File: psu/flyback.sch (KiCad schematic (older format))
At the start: 74 parts

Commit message: Annotate
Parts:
- gave numbers to parts that had none: 74

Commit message: Start PCB
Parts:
- added TP206, TP207: TESTPAD, agg:SIL-254P-01, symbol agg:TESTPAD
- C201: footprint agg:0603 -> agg:1206; Farnell 2320814 -> 1759454; Voltage 16V -> 50V
- C214: value DNF -> 10n; Farnell (none) -> 2896776
- D201, D202: footprint (none) -> agg:SOD-123
- R201, R205: Farnell 2145283 -> 2079442
- R204: value DNF -> 4R7; Farnell (none) -> 2447524
- R213, R214, R215, R216, R222, R223, R224, R225: footprint agg:0805 -> agg:1206; Farnell 2447667 -> 2695162; Voltage 150V -> 200V
- R228: Farnell (none) -> 1717875
- T201: Farnell (none) -> 2458040
- TP203: footprint agg:TESTPAD -> agg:SIL-254P-01
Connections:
- net GND: now also TP206.1 (TP)
- net at C214.2, Q201.D, R206.1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: now also TP207.1 (TP)

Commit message: More PCB
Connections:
- net I_OUT: now also TP205.1 (TP)
- net 390V: now reaches C223.2, C224.2, D205.2, IC205.2, Q202.1 (B), R222.1
- net at C227.1, IC206.3 (+), Q202.3 (C)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: no longer TP205.1 (TP)
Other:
- moved on the sheet: TP205
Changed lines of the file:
@@
 L agg:TESTPAD TP?
 U 1 1 5EB148BA
-P 10250 3200
+P 10400 4850
 AR Path="/5EB148BA" Ref="TP?"  Part="1"
 AR Path="/6147A5D5/5EB148BA" Ref="TP?"  Part="1"
 AR Path="/5D647F49/5EB148BA" Ref="TP205"  Part="1"
-F 0 "TP205" V 10300 3250 50  0000 L CNN
-F 1 "TESTPAD" H 10250 3125 50  0001 L CNN
-F 2 "agg:TESTPAD" H 10250 3050 50  0001 L CNN
-F 3 "" H 10250 3200 50  0001 C CNN
-	1    10250 3200
-	0    1    -1   0
-$EndComp
-Wire Wire Line
-	10250 3200 10250 3250
-Connection ~ 10250 3250
-Wire Wire Line
-	10250 3250 10100 3250
+F 0 "TP205" V 10450 4900 50  0000 L CNN
+F 1 "TESTPAD" H 10400 4775 50  0001 L CNN
+F 2 "agg:TESTPAD" H 10400 4700 50  0001 L CNN
+F 3 "" H 10400 4850 50  0001 C CNN
+	1    10400 4850
+	0    -1   1    0
+$EndComp
 $Comp
 L agg:C C?
@@
 	10500 4050 10500 3250
 Wire Wire Line
-	10250 3250 10500 3250
-Wire Wire Line
 	2100 2900 2100 3650
 Wire Wire Line
@@
 Wire Wire Line
 	4100 3700 4100 3650
+Text Label 8650 2600 2    50   ~ 0
+390V
+Wire Wire Line
+	8650 2600 8750 2600
+Wire Wire Line
+	10400 4850 10400 4750
+Wire Wire Line
+	10100 3250 10500 3250
 $EndSCHEMATC

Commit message: More pcb layout
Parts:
- TP202, TP203, TP206, TP207: footprint agg:SIL-254P-01 -> agg:KEYSTONE5016
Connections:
- net GD: no longer TP202.1 (TP)
- net at IC203.5 (OUT), Q201.G, R203.1: now also TP202.1 (TP)
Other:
- moved on the sheet: TP202
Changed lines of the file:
@@
 Text Notes 3450 2650 0    50   ~ 0
 Gate Driver
-Text HLabel 3000 2900 0    50   Input ~ 0
+Text HLabel 3150 2900 0    50   Input ~ 0
 GD
 Text HLabel 10750 1750 2    50   Output ~ 0
@@
 L agg:TESTPAD TP?
 U 1 1 5D63F412
-P 3100 3000
+P 4050 2700
 AR Path="/5D63F412" Ref="TP?"  Part="1"
 AR Path="/6147A5D5/5D63F412" Ref="TP?"  Part="1"
 AR Path="/5D647F49/5D63F412" Ref="TP202"  Part="1"
-F 0 "TP202" V 3200 3000 50  0000 C CNN
-F 1 "TESTPAD" H 3100 2925 50  0001 L CNN
-F 2 "agg:SIL-254P-01" H 3100 2850 50  0001 L CNN
-F 3 "" H 3100 3000 50  0001 C CNN
-	1    3100 3000
-	0    1    1    0
+F 0 "TP202" V 4150 2700 50  0000 C CNN
+F 1 "TESTPAD" H 4050 2625 50  0001 L CNN
+F 2 "agg:KEYSTONE5016" H 4050 2550 50  0001 L CNN
+F 3 "" H 4050 2700 50  0001 C CNN
+	1    4050 2700
+	0    -1   -1   0
 $EndComp
 $Comp
@@
 	4200 3150 4200 3050
 Wire Wire Line
-	3950 2800 4200 2800
+	3950 2800 4050 2800
 Wire Wire Line
 	4200 2950 4200 2800
@@
 Wire Wire Line
 	5200 1950 5350 1950
-Wire Wire Line
-	3100 3000 3100 2900
-Wire Wire Line
-	3000 2900 3100 2900
-Connection ~ 3100 2900
-Wire Wire Line
-	3100 2900 3350 2900
 $Comp
 L agg:C C?
@@
 F 0 "TP207" V 4500 2450 50  0000 C CNN
 F 1 "TESTPAD" H 4400 2375 50  0001 L CNN
-F 2 "agg:SIL-254P-01" H 4400 2300 50  0001 L CNN
+F 2 "agg:KEYSTONE5016" H 4400 2300 50  0001 L CNN
 F 3 "" H 4400 2450 50  0001 C CNN
 	1    4400 2450
@@
 F 0 "TP203" V 5750 3650 50  0000 C CNN
 F 1 "TESTPAD" H 5650 3575 50  0001 L CNN
-F 2 "agg:SIL-254P-01" H 5650 3500 50  0001 L CNN
+F 2 "agg:KEYSTONE5016" H 5650 3500 50  0001 L CNN
 F 3 "" H 5650 3650 50  0001 C CNN
 	1    5650 3650
@@
 F 0 "TP206" V 4200 3650 50  0000 C CNN
 F 1 "TESTPAD" H 4100 3575 50  0001 L CNN
-F 2 "agg:SIL-254P-01" H 4100 3500 50  0001 L CNN
+F 2 "agg:KEYSTONE5016" H 4100 3500 50  0001 L CNN
 F 3 "" H 4100 3650 50  0001 C CNN
 	1    4100 3650
@@
 Wire Wire Line
 	10100 3250 10500 3250
+Wire Wire Line
+	4050 2700 4050 2800
+Connection ~ 4050 2800
+Wire Wire Line
+	4050 2800 4200 2800
+Wire Wire Line
+	3150 2900 3350 2900
 $EndSCHEMATC

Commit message: routing
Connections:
- net 400V: now reaches C216.2, C219.1, C223.1, C224.1, D203.1, D204.1, IC205.3 (+), IC205.5, R213.1, R218.1, R228.2
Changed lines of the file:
@@
 Wire Wire Line
 	4100 3700 4100 3650
-Text Label 8650 2600 2    50   ~ 0
+Text Label 8750 2600 0    50   ~ 0
 390V
-Wire Wire Line
-	8650 2600 8750 2600
 Wire Wire Line
 	10400 4850 10400 4750
@@
 Wire Wire Line
 	3150 2900 3350 2900
+Text Label 8750 1750 0    50   ~ 0
+400V
 $EndSCHEMATC

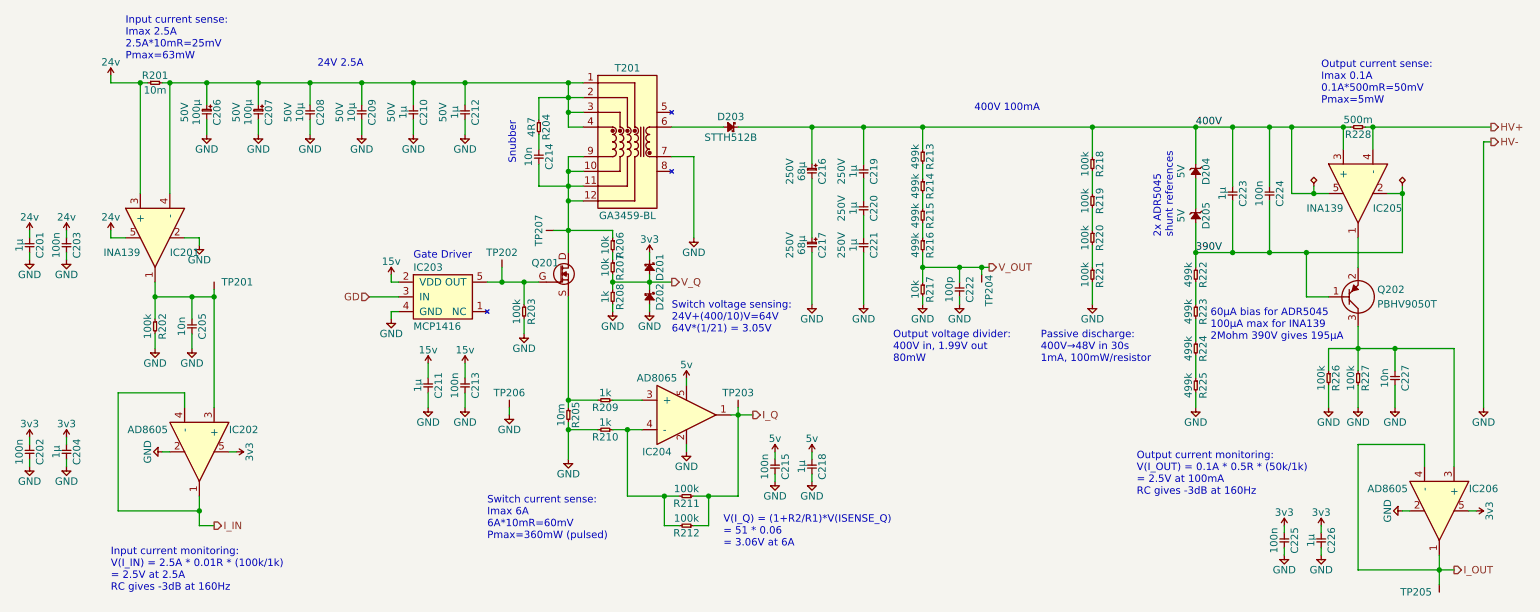
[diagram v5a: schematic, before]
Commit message: Complete routing. But maybe the transformer is the wrong way around.
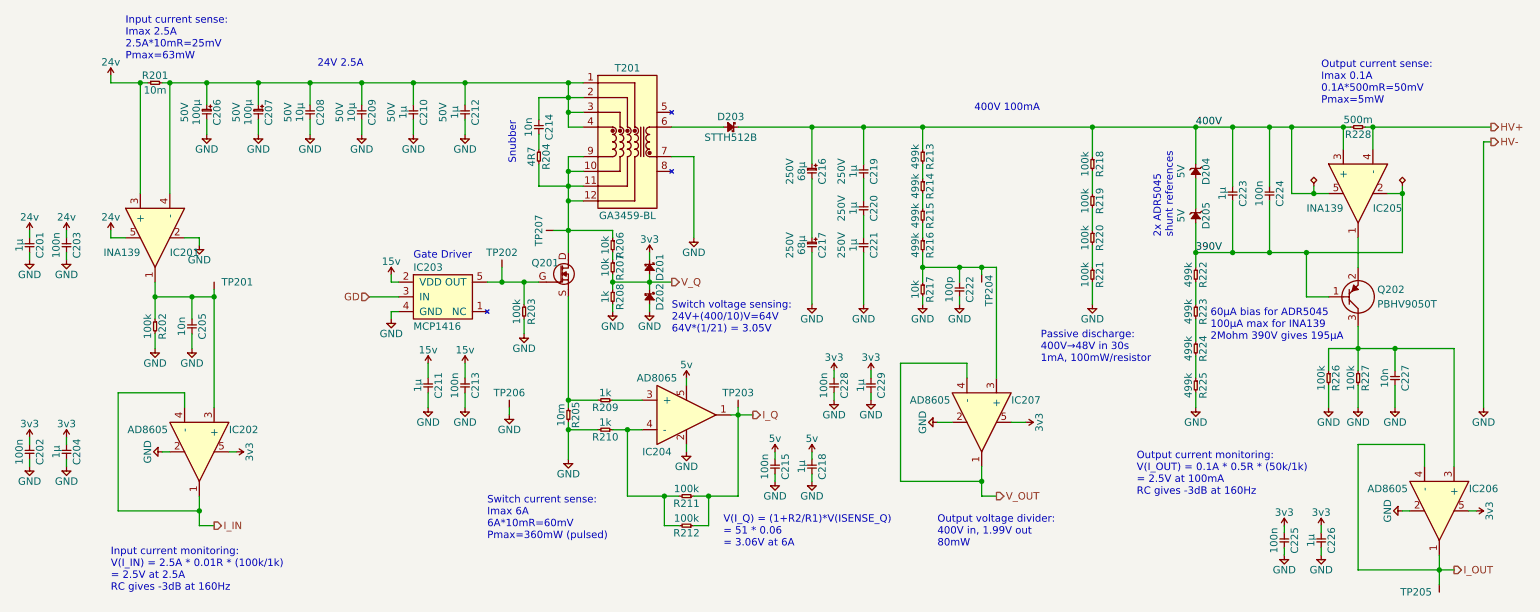
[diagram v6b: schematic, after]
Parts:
- added C228: 100n, agg:0603, symbol agg:C
- added C229: 1µ, agg:0603, symbol agg:C
- added IC207: AD8605, agg:SOT-23-5, symbol agg:AD8605
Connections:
- net 3v3: now also C228.1, C229.1, IC207.5
- net GND: now also C228.2, C229.2, IC207.2
- net V_OUT: now also IC207.1, IC207.4 (-); no longer C222.1, R216.2, R217.1, TP204.1 (TP)
- net at C206.2, C207.2, C208.1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: now also C214.1; no longer R204.1
- net at R204.2: now also Q201.D, R206.1, T201.10, T201.11, T201.12, T201.9, TP207.1 (TP); no longer C214.1
- new net: C214.2, R204.1
- new net: C222.1, IC207.3 (+), R216.2, R217.1, TP204.1 (TP)
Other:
- moved on the sheet: C214, R204
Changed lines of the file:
@@
 L agg:R R?
 U 1 1 5D63EFC1
-P 4300 1700
+P 4300 1900
 AR Path="/5D63EFC1" Ref="R?"  Part="1"
 AR Path="/6147A5D5/5D63EFC1" Ref="R?"  Part="1"
 AR Path="/5D647F49/5D63EFC1" Ref="R204"  Part="1"
-F 0 "R204" H 4350 1750 50  0000 C CNN
-F 1 "4R7" H 4350 1650 50  0000 C CNN
-F 2 "agg:1206" H 4300 1700 50  0001 C CNN
-F 3 "http://www.farnell.com/datasheets/2563624.pdf" H 4300 1700 50  0001 C CNN
-F 4 "50V" H 4300 1700 50  0001 C CNN "Voltage"
-F 5 "2447524" H 4300 1700 50  0001 C CNN "Farnell"
-	1    4300 1700
+F 0 "R204" H 4350 1950 50  0000 C CNN
+F 1 "4R7" H 4350 1850 50  0000 C CNN
+F 2 "agg:1206" H 4300 1900 50  0001 C CNN
+F 3 "http://www.farnell.com/datasheets/2563624.pdf" H 4300 1900 50  0001 C CNN
+F 4 "50V" H 4300 1900 50  0001 C CNN "Voltage"
+F 5 "2447524" H 4300 1900 50  0001 C CNN "Farnell"
+	1    4300 1900
 	0    1    1    0
 $EndComp
@@
 L agg:C C?
 U 1 1 5D63EFC8
-P 4300 1900
+P 4300 1700
 AR Path="/5D63EFC8" Ref="C?"  Part="1"
 AR Path="/6147A5D5/5D63EFC8" Ref="C?"  Part="1"
 AR Path="/5D647F49/5D63EFC8" Ref="C214"  Part="1"
-F 0 "C214" H 4350 1970 50  0000 C CNN
-F 1 "10n" H 4350 1830 50  0000 C CNN
-F 2 "agg:1206" H 4300 1900 50  0001 C CNN
-F 3 "http://www.farnell.com/datasheets/2620236.pdf" H 4300 1900 50  0001 C CNN
-F 4 "50V" H 4300 1900 50  0001 C CNN "Voltage"
-F 5 "2896776" H 4300 1900 50  0001 C CNN "Farnell"
-	1    4300 1900
+F 0 "C214" H 4350 1770 50  0000 C CNN
+F 1 "10n" H 4350 1630 50  0000 C CNN
+F 2 "agg:1206" H 4300 1700 50  0001 C CNN
+F 3 "http://www.farnell.com/datasheets/2620236.pdf" H 4300 1700 50  0001 C CNN
+F 4 "50V" H 4300 1700 50  0001 C CNN "Voltage"
+F 5 "2896776" H 4300 1700 50  0001 C CNN "Farnell"
+	1    4300 1700
 	0    1    1    0
 $EndComp
@@
 Wire Wire Line
 	6900 2700 6900 2800
-Text Notes 6700 3350 0    50   ~ 0
+Text Notes 7000 4600 0    50   ~ 0
 Output voltage divider:\n400V in, 1.99V out\n80mW
 $Comp
@@
 Wire Wire Line
 	7150 2950 7150 2900
-Text HLabel 7350 2700 2    50   Output ~ 0
+Text HLabel 7400 4250 2    50   Output ~ 0
 V_OUT
 Wire Wire Line
@@
 	7300 2750 7300 2700
 Connection ~ 7300 2700
-Wire Wire Line
-	7300 2700 7350 2700
 $Comp
 L agg:TESTPAD TP?
@@
 Text Label 8750 1750 0    50   ~ 0
 400V
+$Comp
+L agg:AD8605 IC207
+U 1 1 5FF25183
+P 7300 3650
+F 0 "IC207" V 7250 3950 50  0000 C CNN
+F 1 "AD8605" V 7250 3300 50  0000 C CNN
+F 2 "agg:SOT-23-5" H 7300 3300 50  0001 C CNN
+F 3 "https://www.analog.com/media/en/technical-documentation/data-sheets/AD8605_8606_8608.pdf" H 7300 3650 50  0001 C CNN
+F 4 "1838870" H 7300 3200 50  0001 C CNN "Farnell"
+	1    7300 3650
+	0    1    1    0
+$EndComp
+Wire Wire Line
+	7300 4050 7300 4150
+Wire Wire Line
+	7300 4150 6750 4150
+Wire Wire Line
+	6750 4150 6750 3350
+Wire Wire Line
+	6750 3350 7200 3350
+Wire Wire Line
+	7200 3350 7200 3450
+$Comp
+L agg:GND #PWR0261
+U 1 1 5FF5B9B1
+P 7000 3750
+F 0 "#PWR0261" H 6870 3790 50  0001 L CNN
+F 1 "GND" H 7000 3650 50  0000 C CNN
+F 2 "" H 7000 3750 50  0001 C CNN
+F 3 "" H 7000 3750 50  0001 C CNN
+	1    7000 3750
+	0    1    1    0
+$EndComp
+Wire Wire Line
+	7000 3750 7100 3750
+$Comp
+L agg:3v3 #PWR0262
+U 1 1 5FF6D004
+P 7600 3750
+F 0 "#PWR0262" H 7600 3860 50  0001 L CNN
+F 1 "3v3" H 7600 3840 50  0000 C CNN
+F 2 "" H 7600 3750 50  0001 C CNN
+F 3 "" H 7600 3750 50  0001 C CNN
+	1    7600 3750
+	0    1    1    0
+$EndComp
+Wire Wire Line
+	7600 3750 7500 3750
+Wire Wire Line
+	7400 3450 7400 2700
+Wire Wire Line
+	7300 2700 7400 2700
+Wire Wire Line
+	7300 4150 7300 4250
+Wire Wire Line
+	7300 4250 7400 4250
+Connection ~ 7300 4150
+$Comp
+L agg:C C?
+U 1 1 5FFAEEFA
+P 6300 3450
+AR Path="/5FFAEEFA" Ref="C?"  Part="1"
+AR Path="/6147A5D5/5FFAEEFA" Ref="C?"  Part="1"
+AR Path="/5D647F49/5FFAEEFA" Ref="C228"  Part="1"
+F 0 "C228" H 6350 3520 50  0000 C CNN
+F 1 "100n" H 6350 3380 50  0000 C CNN
+F 2 "agg:0603" H 6300 3450 50  0001 C CNN
+F 3 "" H 6300 3450 50  0001 C CNN
+F 4 "50V" H 6300 3450 50  0001 C CNN "Voltage"
+F 5 "2320803" H 6300 3450 50  0001 C CNN "Farnell"
+	1    6300 3450
+	0    1    1    0
+$EndComp
+$Comp
+L agg:C C?
+U 1 1 5FFAEF06
+P 6550 3450
+AR Path="/5FFAEF06" Ref="C?"  Part="1"
+AR Path="/6147A5D5/5FFAEF06" Ref="C?"  Part="1"
+AR Path="/5D647F49/5FFAEF06" Ref="C229"  Part="1"
+F 0 "C229" H 6600 3520 50  0000 C CNN
+F 1 "1µ" H 6600 3380 50  0000 C CNN
+F 2 "agg:0603" H 6550 3450 50  0001 C CNN
+F 3 "" H 6550 3450 50  0001 C CNN
+F 4 "16V" H 6550 3450 50  0001 C CNN "Voltage"
+F 5 "2320814" H 6550 3450 50  0001 C CNN "Farnell"
+	1    6550 3450
+	0    1    1    0
+$EndComp
+$Comp
+L agg:3v3 #PWR?
+U 1 1 5FFAEF10
+P 6550 3400
+AR Path="/5FFAEF10" Ref="#PWR?"  Part="1"
+AR Path="/6147A5D5/5FFAEF10" Ref="#PWR?"  Part="1"
+AR Path="/5D647F49/5FFAEF10" Ref="#PWR0259"  Part="1"
+F 0 "#PWR0259" H 6550 3510 50  0001 L CNN
+F 1 "3v3" H 6550 3490 50  0000 C CNN
+F 2 "" H 6550 3400 50  0001 C CNN
+F 3 "" H 6550 3400 50  0001 C CNN
+	1    6550 3400
+	1    0    0    -1
+$EndComp
+$Comp
+L agg:3v3 #PWR?
+U 1 1 5FFAEF1A
+P 6300 3400
+AR Path="/5FFAEF1A" Ref="#PWR?"  Part="1"
+AR Path="/6147A5D5/5FFAEF1A" Ref="#PWR?"  Part="1"
+AR Path="/5D647F49/5FFAEF1A" Ref="#PWR0257"  Part="1"
+F 0 "#PWR0257" H 6300 3510 50  0001 L CNN
+F 1 "3v3" H 6300 3490 50  0000 C CNN
+F 2 "" H 6300 3400 50  0001 C CNN
+F 3 "" H 6300 3400 50  0001 C CNN
+	1    6300 3400
+	1    0    0    -1
+$EndComp
+$Comp
+L agg:GND #PWR?
+U 1 1 5FFAEF24
+P 6300 3600
+AR Path="/5FFAEF24" Ref="#PWR?"  Part="1"
+AR Path="/6147A5D5/5FFAEF24" Ref="#PWR?"  Part="1"
+AR Path="/5D647F49/5FFAEF24" Ref="#PWR0258"  Part="1"
+F 0 "#PWR0258" H 6170 3640 50  0001 L CNN
+F 1 "GND" H 6300 3500 50  0000 C CNN
+F 2 "" H 6300 3600 50  0001 C CNN
+F 3 "" H 6300 3600 50  0001 C CNN
+	1    6300 3600
+	1    0    0    -1
+$EndComp
+$Comp
+L agg:GND #PWR?
+U 1 1 5FFAEF2E
+P 6550 3600
+AR Path="/5FFAEF2E" Ref="#PWR?"  Part="1"
+AR Path="/6147A5D5/5FFAEF2E" Ref="#PWR?"  Part="1"
+AR Path="/5D647F49/5FFAEF2E" Ref="#PWR0260"  Part="1"
+F 0 "#PWR0260" H 6420 3640 50  0001 L CNN
+F 1 "GND" H 6550 3500 50  0000 C CNN
+F 2 "" H 6550 3600 50  0001 C CNN
+F 3 "" H 6550 3600 50  0001 C CNN
+	1    6550 3600
+	1    0    0    -1
+$EndComp
+Wire Wire Line
+	6550 3600 6550 3550
+Wire Wire Line
+	6550 3450 6550 3400
+Wire Wire Line
+	6300 3400 6300 3450
+Wire Wire Line
+	6300 3550 6300 3600
 $EndSCHEMATC

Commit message: Complete routing take 2, with transformer secondary pins swapped
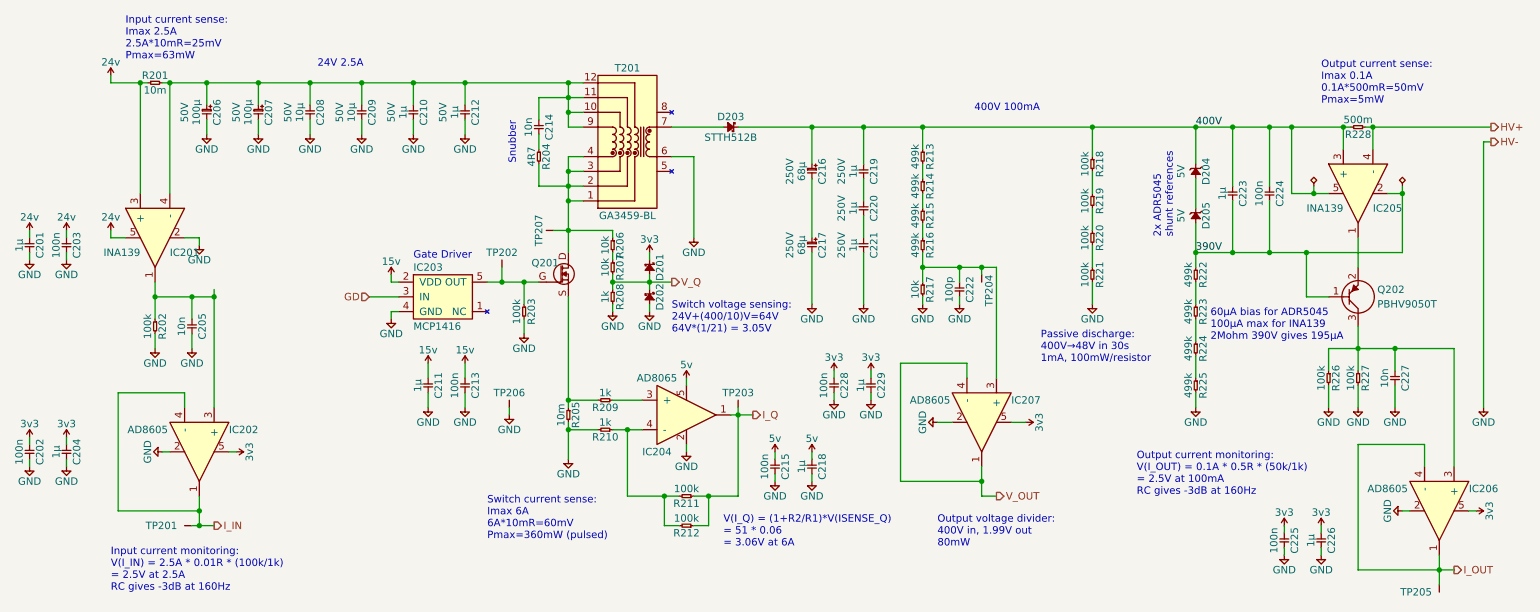
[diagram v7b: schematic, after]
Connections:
- net GND: now also T201.6; no longer T201.7
- net I_IN: now also TP201.1 (TP)
- net at C206.2, C207.2, C208.1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: now also T201.10, T201.11, T201.12, T201.9; no longer T201.1, T201.2, T201.3, T201.4
- net at D203.2: now also T201.7; no longer T201.6
- net at Q201.D, R204.2, R206.1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: now also T201.1, T201.2, T201.3, T201.4; no longer T201.10, T201.11, T201.12, T201.9
- net at C205.1, IC201.1, IC202.3 (+)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: no longer TP201.1 (TP)
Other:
- moved on the sheet: TP201
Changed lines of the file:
@@
 L agg:TESTPAD TP?
 U 1 1 5D63F43C
-P 2100 2850
+P 1950 4450
 AR Path="/5D63F43C" Ref="TP?"  Part="1"
 AR Path="/6147A5D5/5D63F43C" Ref="TP?"  Part="1"
 AR Path="/5D647F49/5D63F43C" Ref="TP201"  Part="1"
-F 0 "TP201" V 2150 2900 50  0000 L CNN
-F 1 "TESTPAD" H 2100 2775 50  0001 L CNN
-F 2 "agg:TESTPAD" H 2100 2700 50  0001 L CNN
-F 3 "" H 2100 2850 50  0001 C CNN
-	1    2100 2850
-	0    1    -1   0
+F 0 "TP201" H 2050 4450 50  0000 L CNN
+F 1 "TESTPAD" H 1950 4375 50  0001 L CNN
+F 2 "agg:TESTPAD" H 1950 4300 50  0001 L CNN
+F 3 "" H 1950 4450 50  0001 C CNN
+	1    1950 4450
+	-1   0    0    1
 $EndComp
 $Comp
@@
 U 1 1 5D742CF1
 P 4900 1850
-F 0 "T201" H 4900 2350 50  0000 C CNN
-F 1 "GA3459-BL" H 4900 1350 50  0000 C CNN
+F 0 "T201" H 4900 1350 50  0000 C CNN
+F 1 "GA3459-BL" H 4900 2350 50  0000 C CNN
 F 2 "agg:GA3459-BL" H 4900 1250 50  0001 C CNN
 F 3 "https://www.coilcraft.com/pdfs/ga3459.pdf" H 4800 1850 50  0001 C CNN
 F 4 "2458040" H 4900 1850 50  0001 C CNN "Farnell"
 	1    4900 1850
-	1    0    0    -1
+	1    0    0    1
 $EndComp
 Wire Wire Line
@@
 Wire Wire Line
 	6300 3550 6300 3600
+Wire Wire Line
+	1950 4450 2000 4450
+Connection ~ 2000 4450
 $EndSCHEMATC

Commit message: Update Farnell part numbers
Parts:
- TP202, TP203, TP206, TP207: Farnell (none) -> 2292858
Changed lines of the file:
@@
 F 2 "agg:KEYSTONE5016" H 4050 2550 50  0001 L CNN
 F 3 "" H 4050 2700 50  0001 C CNN
+F 4 "2292858" H 4050 2700 50  0001 C CNN "Farnell"
 	1    4050 2700
 	0    -1   -1   0
@@
 F 2 "agg:KEYSTONE5016" H 4400 2300 50  0001 L CNN
 F 3 "" H 4400 2450 50  0001 C CNN
+F 4 "2292858" H 4400 2450 50  0001 C CNN "Farnell"
 	1    4400 2450
 	-1   0    0    1
@@
 F 2 "agg:KEYSTONE5016" H 5650 3500 50  0001 L CNN
 F 3 "" H 5650 3650 50  0001 C CNN
+F 4 "2292858" H 5650 3650 50  0001 C CNN "Farnell"
 	1    5650 3650
 	0    -1   -1   0
@@
 F 2 "agg:KEYSTONE5016" H 4100 3500 50  0001 L CNN
 F 3 "" H 4100 3650 50  0001 C CNN
+F 4 "2292858" H 4100 3650 50  0001 C CNN "Farnell"
 	1    4100 3650
 	0    -1   -1   0
